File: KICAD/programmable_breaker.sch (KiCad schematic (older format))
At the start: 38 parts

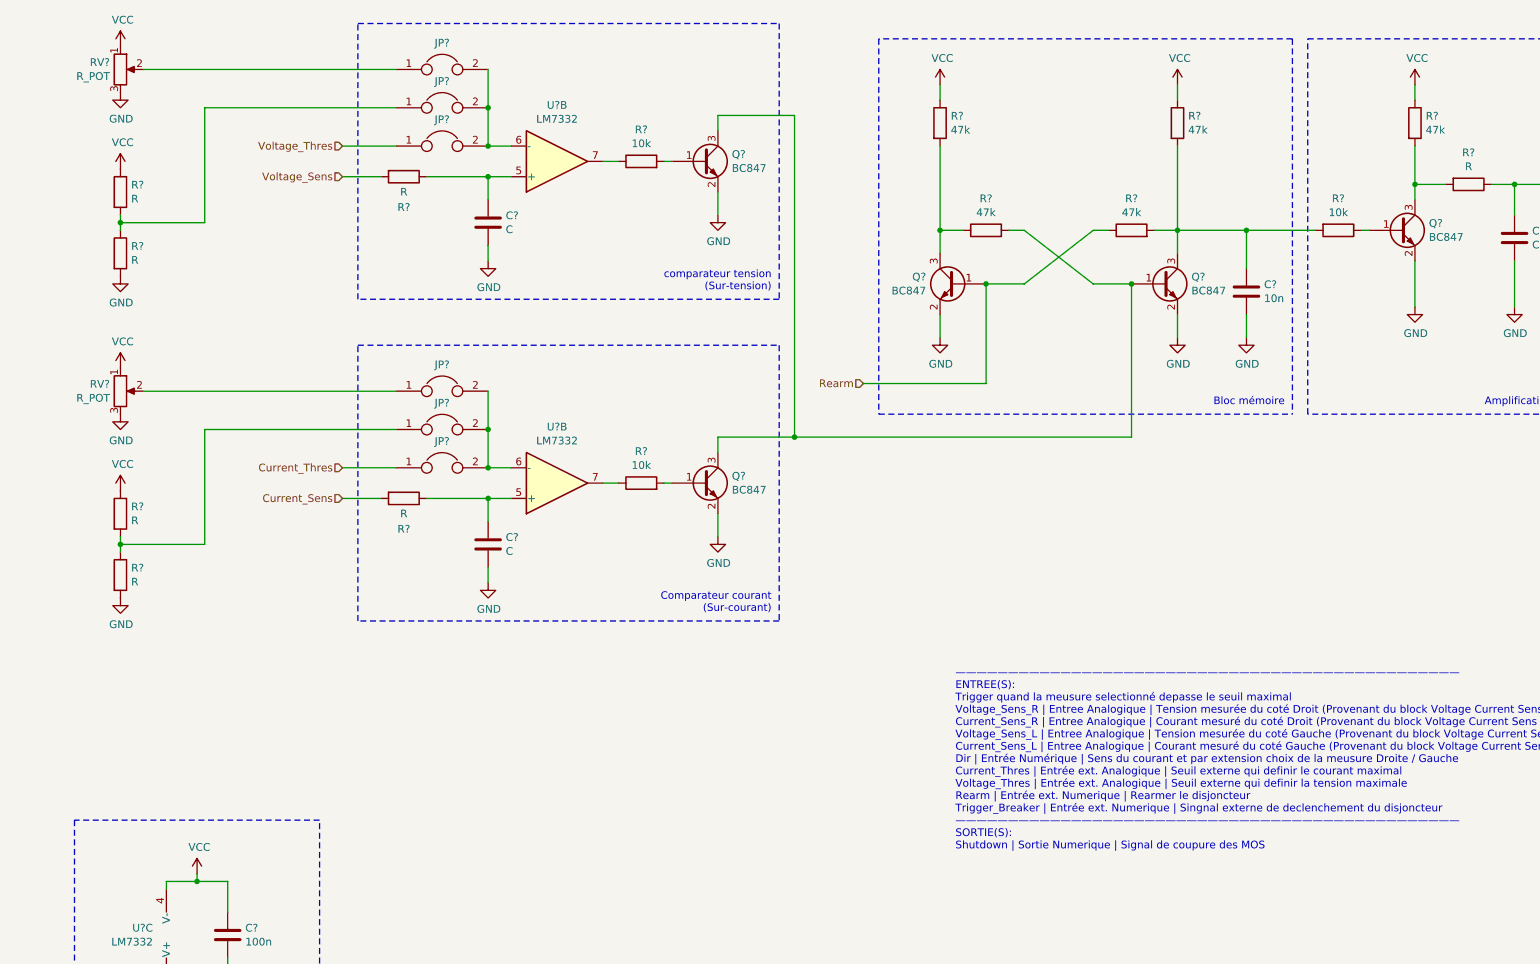
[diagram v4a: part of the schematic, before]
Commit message: minors edits + 7v rail
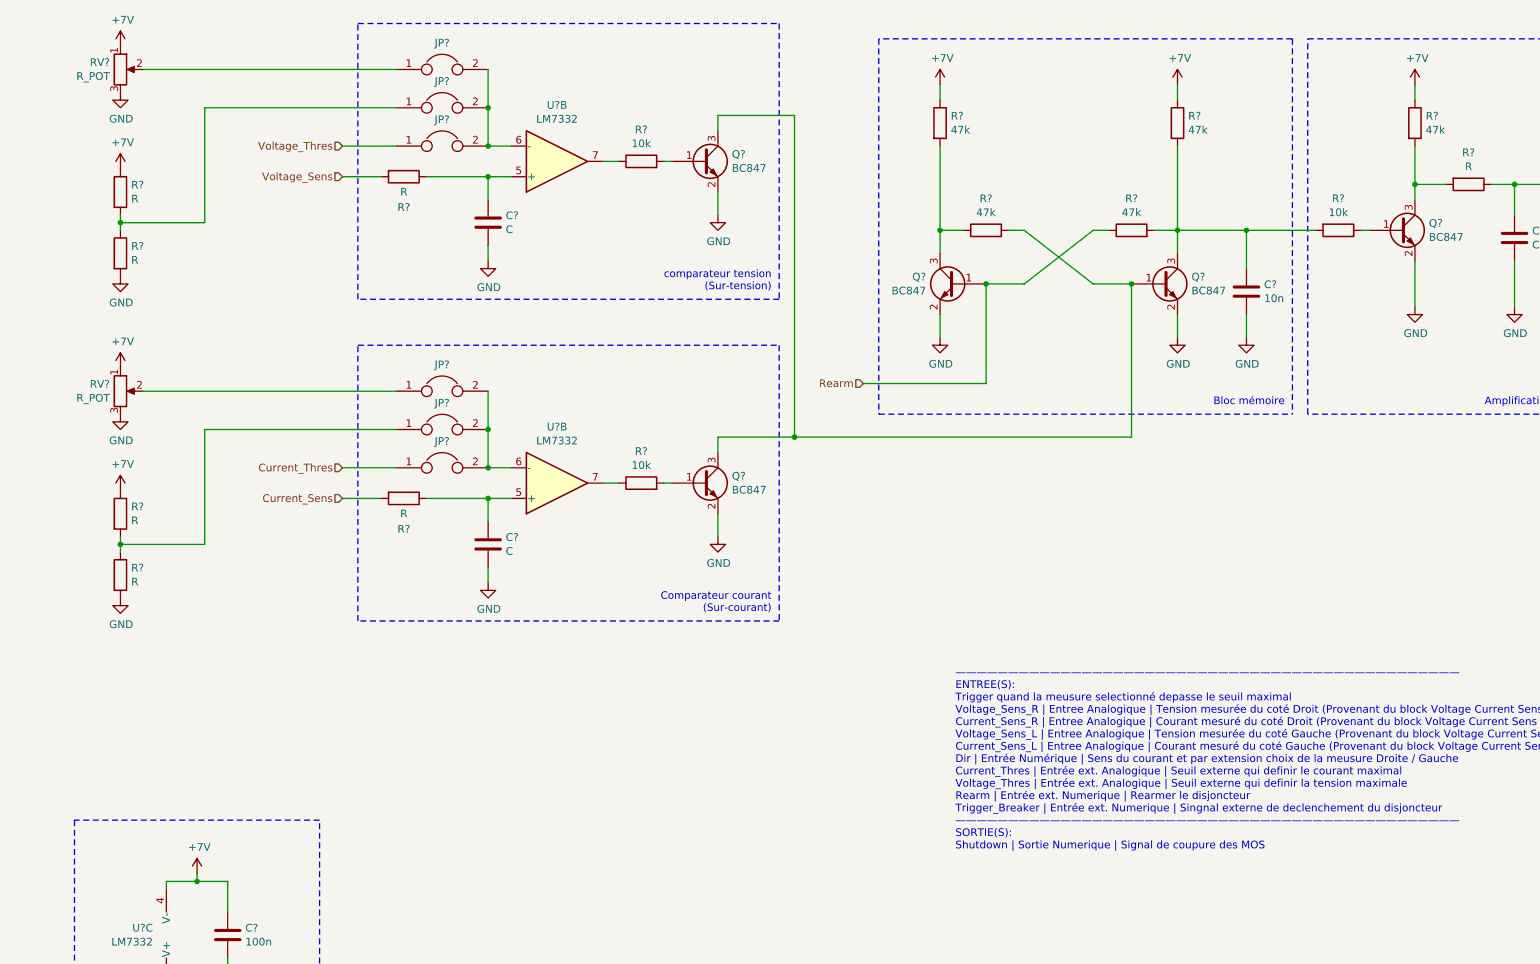
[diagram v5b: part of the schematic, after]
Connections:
- net VCC renamed +7V
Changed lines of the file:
@@
 Wire Notes Line
 	5900 3400 8600 3400
-$Comp
-L power:VCC #PWR?
-U 1 1 610F372F
-P 7850 1250
-F 0 "#PWR?" H 7850 1100 50  0001 C CNN
-F 1 "VCC" H 7865 1423 50  0000 C CNN
-F 2 "" H 7850 1250 50  0001 C CNN
-F 3 "" H 7850 1250 50  0001 C CNN
-	1    7850 1250
-	1    0    0    -1
-$EndComp
 Wire Wire Line
 	7850 1250 7850 1350
-$Comp
-L power:VCC #PWR?
-U 1 1 6110D98E
-P 6300 1250
-F 0 "#PWR?" H 6300 1100 50  0001 C CNN
-F 1 "VCC" H 6315 1423 50  0000 C CNN
-F 2 "" H 6300 1250 50  0001 C CNN
-F 3 "" H 6300 1250 50  0001 C CNN
-	1    6300 1250
-	1    0    0    -1
-$EndComp
 Wire Wire Line
 	6300 1250 6300 1350
-$Comp
-L power:VCC #PWR?
-U 1 1 611109FE
-P 9400 1250
-F 0 "#PWR?" H 9400 1100 50  0001 C CNN
-F 1 "VCC" H 9415 1423 50  0000 C CNN
-F 2 "" H 9400 1250 50  0001 C CNN
-F 3 "" H 9400 1250 50  0001 C CNN
-	1    9400 1250
-	1    0    0    -1
-$EndComp
 Wire Wire Line
 	9400 1250 9400 1350
@@
 Text HLabel 2400 3750 0    50   Input ~ 0
 Current_Thres
-$Comp
-L power:VCC #PWR?
-U 1 1 611A0736
-P 950 3900
-F 0 "#PWR?" H 950 3750 50  0001 C CNN
-F 1 "VCC" H 965 4073 50  0000 C CNN
-F 2 "" H 950 3900 50  0001 C CNN
-F 3 "" H 950 3900 50  0001 C CNN
-	1    950  3900
-	1    0    0    -1
-$EndComp
-$Comp
-L power:VCC #PWR?
-U 1 1 611A1208
-P 950 3100
-F 0 "#PWR?" H 950 2950 50  0001 C CNN
-F 1 "VCC" H 965 3273 50  0000 C CNN
-F 2 "" H 950 3100 50  0001 C CNN
-F 3 "" H 950 3100 50  0001 C CNN
-	1    950  3100
-	1    0    0    -1
-$EndComp
 $Comp
 L Device:R R?
@@
 $EndComp
 $Comp
-L power:VCC #PWR?
-U 1 1 611DFB38
-P 950 1800
-F 0 "#PWR?" H 950 1650 50  0001 C CNN
-F 1 "VCC" H 965 1973 50  0000 C CNN
-F 2 "" H 950 1800 50  0001 C CNN
-F 3 "" H 950 1800 50  0001 C CNN
-	1    950  1800
-	1    0    0    -1
-$EndComp
-$Comp
-L power:VCC #PWR?
-U 1 1 611DFB3E
-P 950 1000
-F 0 "#PWR?" H 950 850 50  0001 C CNN
-F 1 "VCC" H 965 1173 50  0000 C CNN
-F 2 "" H 950 1000 50  0001 C CNN
-F 3 "" H 950 1000 50  0001 C CNN
-	1    950  1000
-	1    0    0    -1
-$EndComp
-$Comp
 L Device:R R?
 U 1 1 611DFB44
@@
 Wire Wire Line
 	1250 6450 1450 6450
-$Comp
-L power:VCC #PWR?
-U 1 1 612758FE
+Wire Wire Line
+	1450 6400 1450 6450
+Connection ~ 1450 6450
+Wire Wire Line
+	1450 6450 1650 6450
+$Comp
+L Sesame:+7V #PWR?
+U 1 1 6127FC51
+P 9400 1250
+F 0 "#PWR?" H 9400 1100 50  0001 C CNN
+F 1 "+7V" H 9415 1423 50  0000 C CNN
+F 2 "" H 9400 1250 50  0001 C CNN
+F 3 "" H 9400 1250 50  0001 C CNN
+	1    9400 1250
+	1    0    0    -1
+$EndComp
+$Comp
+L Sesame:+7V #PWR?
+U 1 1 61288A44
+P 7850 1250
+F 0 "#PWR?" H 7850 1100 50  0001 C CNN
+F 1 "+7V" H 7865 1423 50  0000 C CNN
+F 2 "" H 7850 1250 50  0001 C CNN
+F 3 "" H 7850 1250 50  0001 C CNN
+	1    7850 1250
+	1    0    0    -1
+$EndComp
+$Comp
+L Sesame:+7V #PWR?
+U 1 1 6128902B
+P 6300 1250
+F 0 "#PWR?" H 6300 1100 50  0001 C CNN
+F 1 "+7V" H 6315 1423 50  0000 C CNN
+F 2 "" H 6300 1250 50  0001 C CNN
+F 3 "" H 6300 1250 50  0001 C CNN
+	1    6300 1250
+	1    0    0    -1
+$EndComp
+$Comp
+L Sesame:+7V #PWR?
+U 1 1 6128C7AA
 P 1450 6400
 F 0 "#PWR?" H 1450 6250 50  0001 C CNN
-F 1 "VCC" H 1465 6573 50  0000 C CNN
+F 1 "+7V" H 1465 6573 50  0000 C CNN
 F 2 "" H 1450 6400 50  0001 C CNN
 F 3 "" H 1450 6400 50  0001 C CNN
@@
 	1    0    0    -1
 $EndComp
-Wire Wire Line
-	1450 6400 1450 6450
-Connection ~ 1450 6450
-Wire Wire Line
-	1450 6450 1650 6450
+$Comp
+L Sesame:+7V #PWR?
+U 1 1 6129AD10
+P 950 1000
+F 0 "#PWR?" H 950 850 50  0001 C CNN
+F 1 "+7V" H 965 1173 50  0000 C CNN
+F 2 "" H 950 1000 50  0001 C CNN
+F 3 "" H 950 1000 50  0001 C CNN
+	1    950  1000
+	1    0    0    -1
+$EndComp
+$Comp
+L Sesame:+7V #PWR?
+U 1 1 6129BC6E
+P 950 1800
+F 0 "#PWR?" H 950 1650 50  0001 C CNN
+F 1 "+7V" H 965 1973 50  0000 C CNN
+F 2 "" H 950 1800 50  0001 C CNN
+F 3 "" H 950 1800 50  0001 C CNN
+	1    950  1800
+	1    0    0    -1
+$EndComp
+$Comp
+L Sesame:+7V #PWR?
+U 1 1 6129C6FF
+P 950 3100
+F 0 "#PWR?" H 950 2950 50  0001 C CNN
+F 1 "+7V" H 965 3273 50  0000 C CNN
+F 2 "" H 950 3100 50  0001 C CNN
+F 3 "" H 950 3100 50  0001 C CNN
+	1    950  3100
+	1    0    0    -1
+$EndComp
+$Comp
+L Sesame:+7V #PWR?
+U 1 1 6129D19F
+P 950 3900
+F 0 "#PWR?" H 950 3750 50  0001 C CNN
+F 1 "+7V" H 965 4073 50  0000 C CNN
+F 2 "" H 950 3900 50  0001 C CNN
+F 3 "" H 950 3900 50  0001 C CNN
+	1    950  3900
+	1    0    0    -1
+$EndComp
 $EndSCHEMATC

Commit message: a ton of new stuff. V0.8
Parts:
- removed C? (x2): C, symbol Device:C
- removed JP? (x3): Jumper, symbol Device:Jumper
- removed Q?: BC847, Package_TO_SOT_SMD:SOT-23, symbol Transistor_BJT:BC847
- removed R? (x4): R, symbol Device:R
- removed R?: 10k, symbol Device:R
- removed RV?: R_POT, symbol Device:R_POT
- removed U?: LM7332, symbol Amplifier_Operational:LM7332
- added C? (x2): 100n, symbol Device:C
- added C?: C, symbol Device:C
- added JP? (x3): Jumper, symbol Device:Jumper
- added Q?: BC847, Package_TO_SOT_SMD:SOT-23, symbol Transistor_BJT:BC847
- added R? (x6): 100k, symbol Device:R
- added R? (x3): R, symbol Device:R
- added R?: 10k, symbol Device:R
- added RV?: R_POT, symbol Device:R_POT
- added U?: LM7332, symbol Amplifier_Operational:LM7332
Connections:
- net Current_Sens: now also R?.2
- net Current_Thres: now also R?.2
- net GND: now also C?.2, Q?.2 (E), R?.2, RV?.3
- net Over_UI_Protection: now also Q?.3 (C), R?.2
- net Voltage_Thres: now also R?.2; no longer JP?.1
- net S: now reaches Q?.1 (B), Q?.3 (C), R?.2
- net S: now also Q?.3 (C)
- net at C?.1, R?.1: now also U?.3 (+); no longer U?.5 (+)
- net at R?.1: now also U?.1; no longer U?.7
- net at JP?.2, JP?.2, JP?.2: now also U?.2 (-), C?.2; no longer U?.6 (-)
- net at JP?.1: now also R?.1; no longer RV?.2
- net at R?.1, R?.2: now also R?.2; no longer JP?.1
- net +7V renamed VCC
- net VCC: no longer R?.1, RV?.1
- new net: JP?.1, R?.1 (x5)
- new net: R?.2, RV?.2 (x2)
- new net: C?.1, R?.1, U?.3 (+)
- new net: R?.1, U?.1
- new net: Q?.1 (B), R?.2
- new net: C?.2, JP?.2, JP?.2, JP?.2, U?.2 (-)
- new net: R?.1, R?.2, R?.2
- new net VREF: C?.1, C?.1, R?.1, R?.1, RV?.1, RV?.1
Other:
- note added: "Col. ouvert ?"
- note added: "Inversion + amplification du signal"
- note added: "Seuil Fixe\nInterne"
- note added: "Seuil Potentiometre\nInterne"
- note added: "Softstart > 10ms a 100ms (le plus lent)"
- note added: "Tres petit (Pics intempestifs) env 1ms"
- note removed: "Amplification du signal de memoire"
- note removed: "Comparateur courant\n(Sur-courant)"
- moved on the sheet: C?, JP?, Q?, R?, SLD1B, SLD2A, U?C
